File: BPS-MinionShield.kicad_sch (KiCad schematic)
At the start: 78 parts, among them J1 Conn_01x18_Female, J14 TempConn2, J9 TempConn2

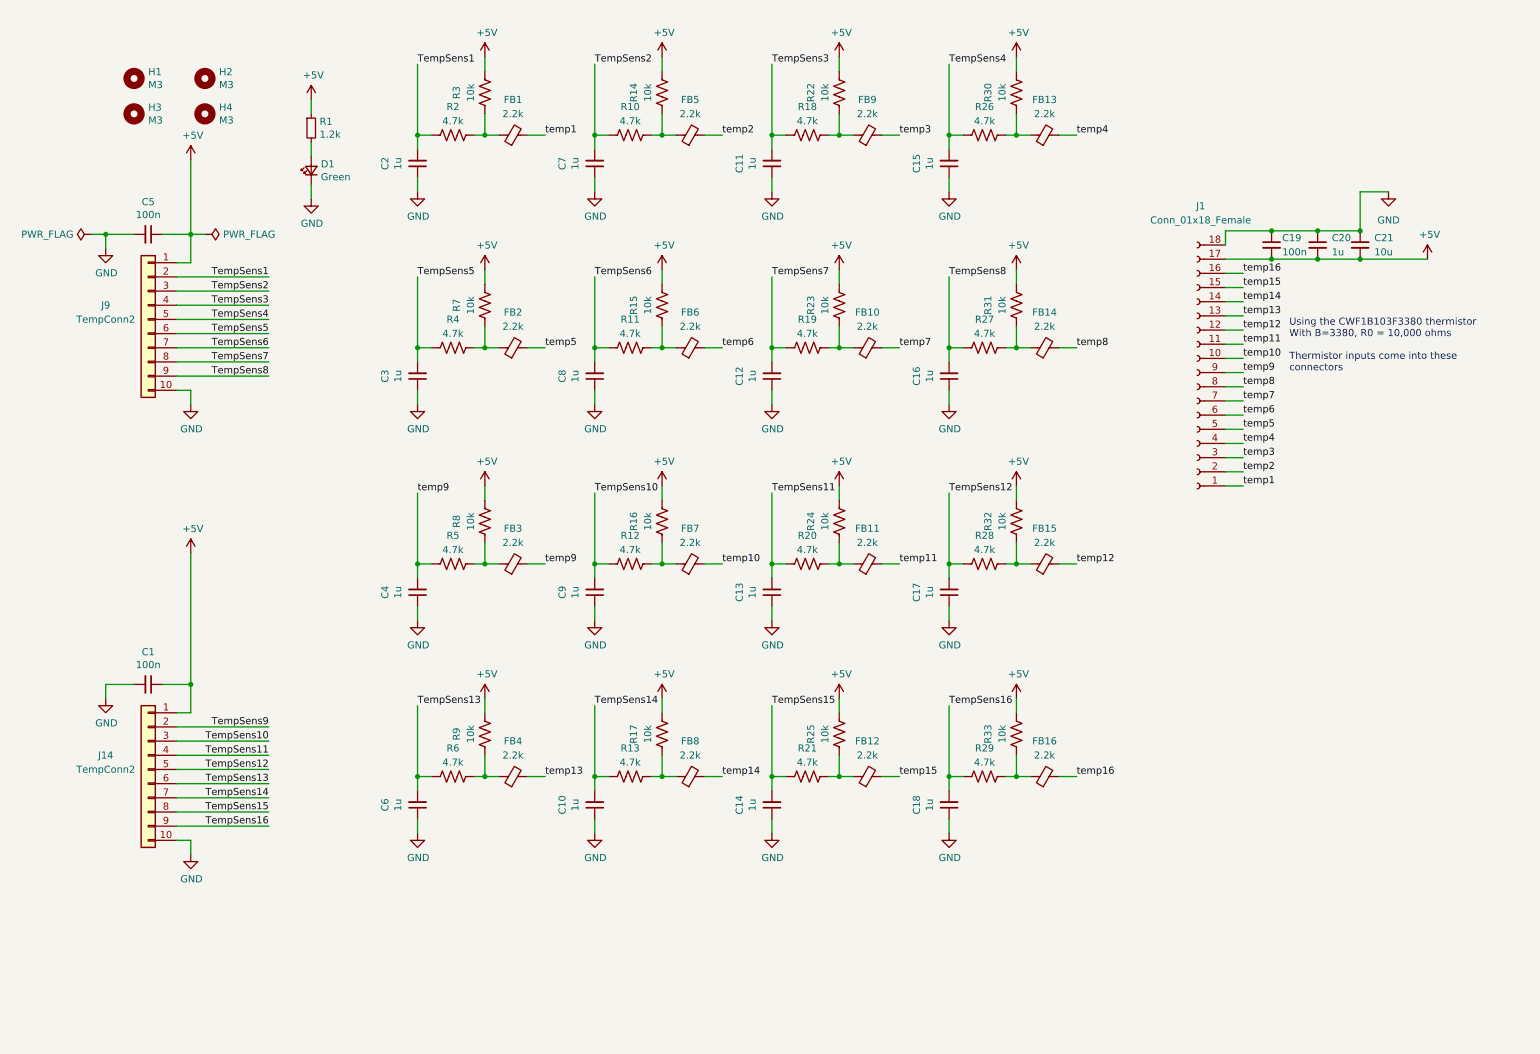
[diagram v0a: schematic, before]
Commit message: added tvs diodes
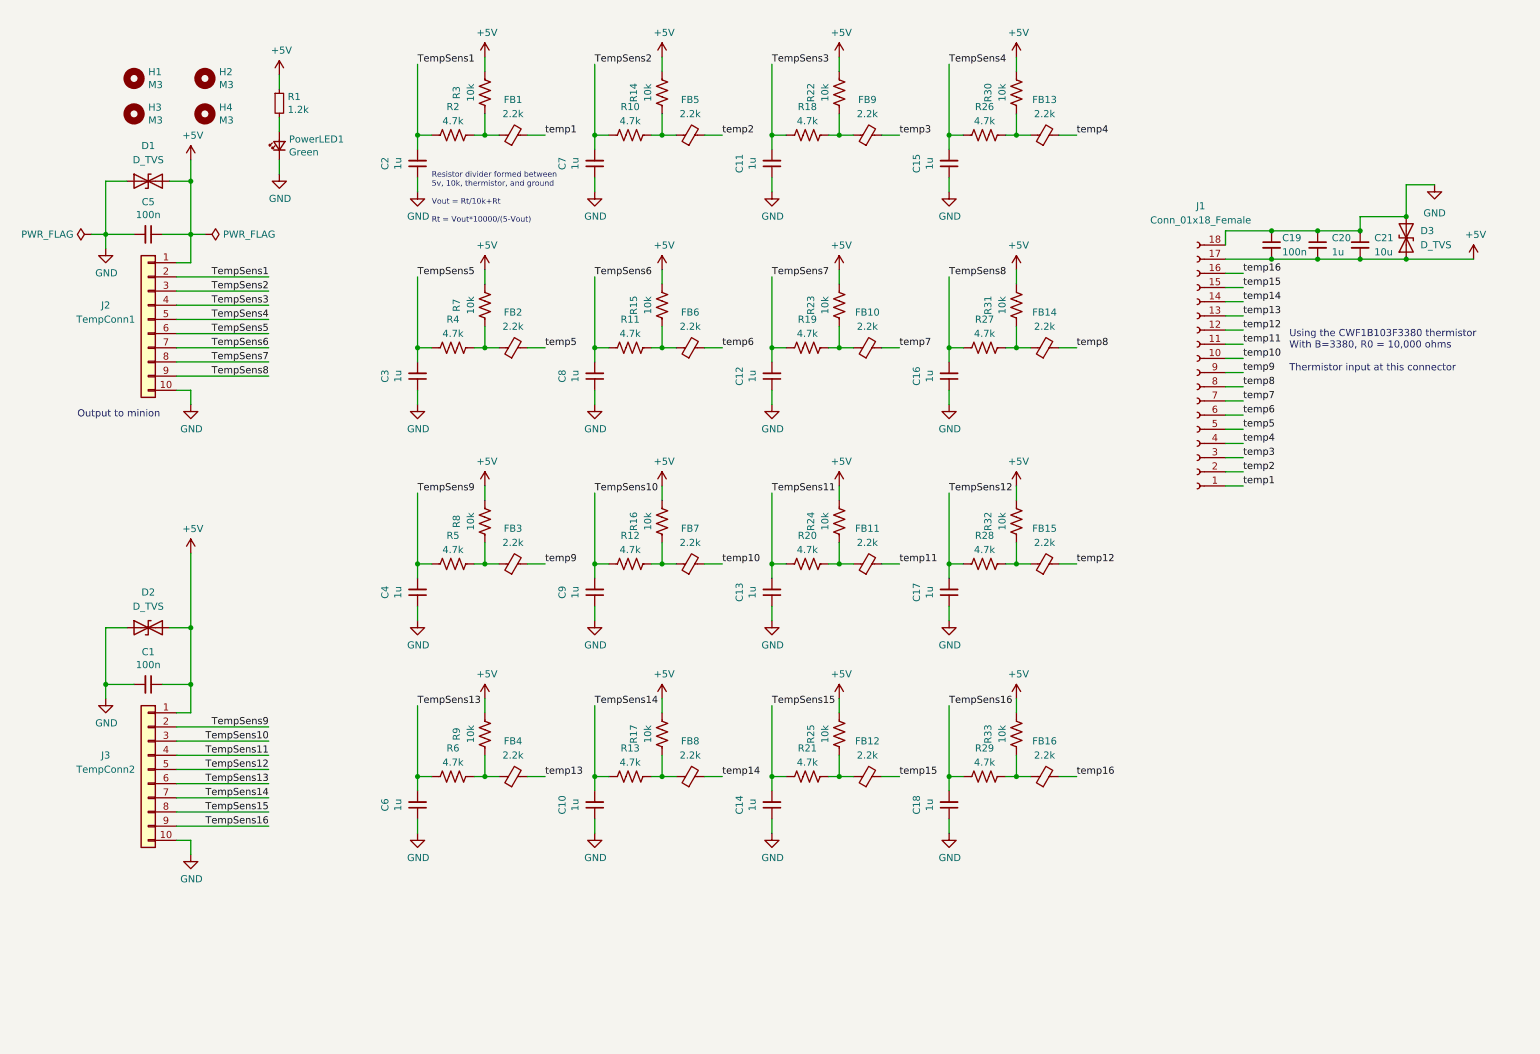
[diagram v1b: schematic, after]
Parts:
- added D1, D2, D3: D_TVS, Diode_SMD:D_0402_1005Metric, symbol Device:D_TVS
- J2: renamed from J9; value TempConn2 -> TempConn1
- renumbered J14 to J3, D1 to PowerLED1
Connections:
- net +5V: now also D1.2 (A2), D2.2 (A2), D3.1 (A1)
- net GND: now also D1.1 (A1), D2.1 (A1), D3.2 (A2)
- net TempSens9: now also C4.2, R5.1
- net temp9: no longer C4.2, R5.1
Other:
- note added: "Output to minion"
- note added: "Resistor divider formed between 5v, 10k, thermistor, and ground Vout = Rt/10k+Rt Rt = Vout*10000/(5-Vout)"
- note added: "Using the CWF1B103F3380 thermistor With B=3380, R0 = 10,000 ohms Thermistor input at this connector"
- note removed: "Using the CWF1B103F3380 thermistor With B=3380, R0 = 10,000 ohms Thermistor inputs come into these connectors"
- moved on the sheet: PowerLED1, R1

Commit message: finished PCB layout with a displayport connector for thermistors
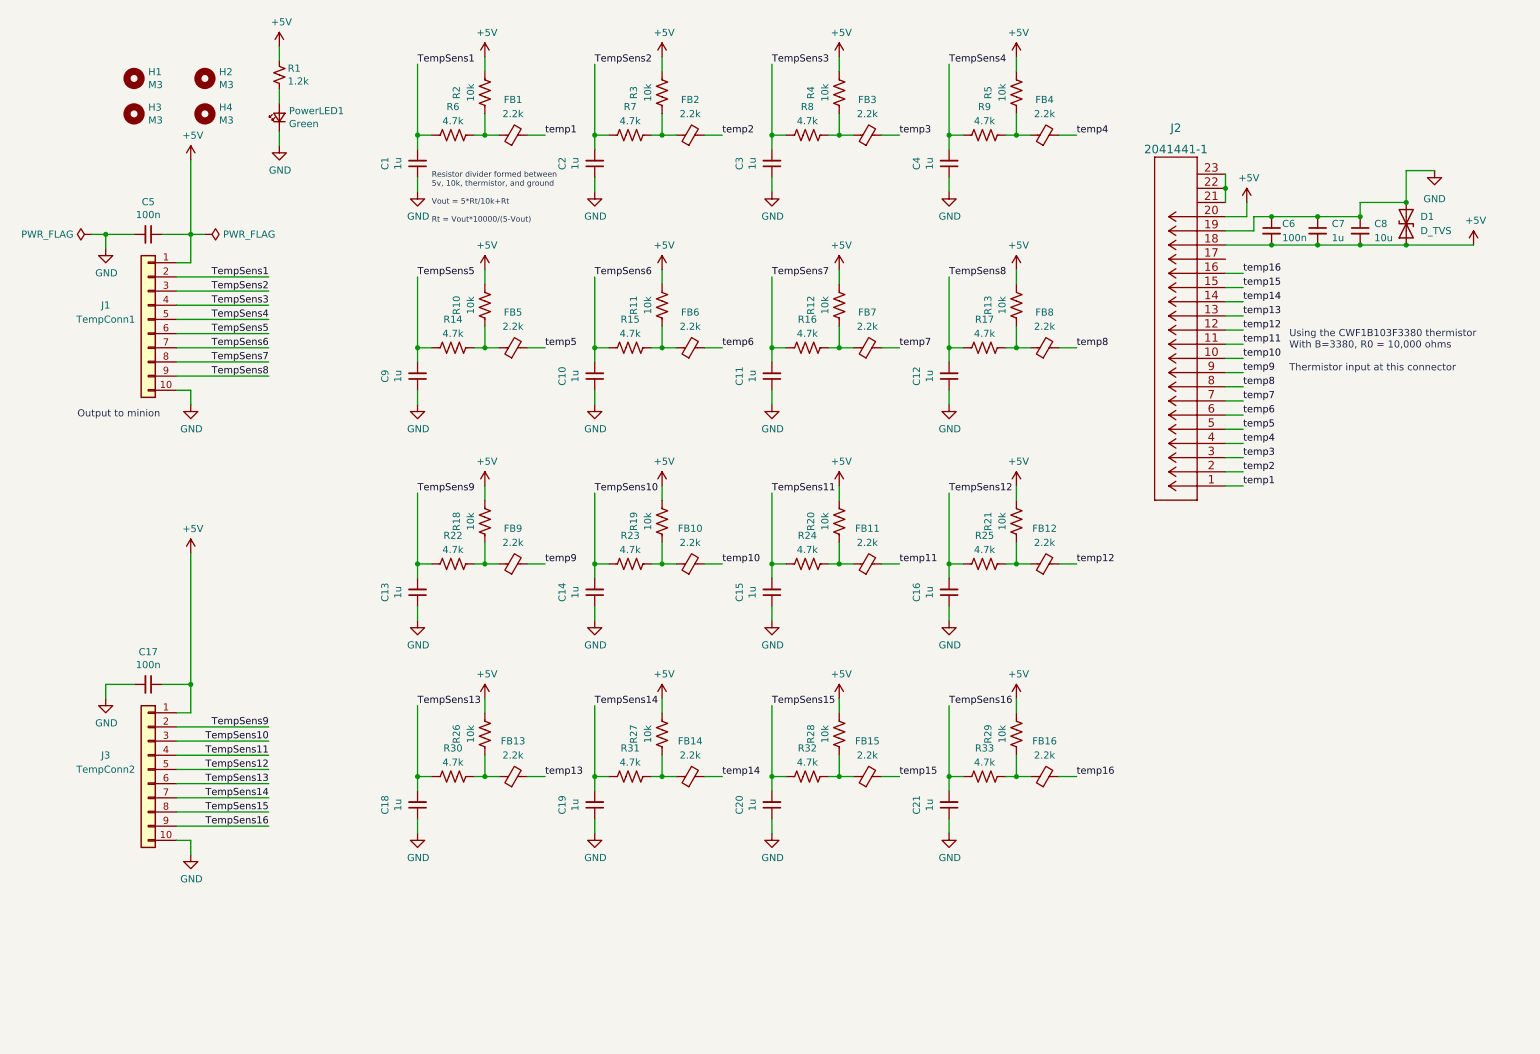
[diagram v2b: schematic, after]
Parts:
- removed D1, D2: D_TVS, Diode_SMD:D_0402_1005Metric, symbol Device:D_TVS
- removed J1: Conn_01x18_Female, symbol Connector:Conn_01x18_Female
- added J2: 2041441-1, UTSVT_Connectors:2041441-1, symbol displayport:2041441-1
- R1: symbol Device:R_Small -> Device:R_Small_US
- renumbered C2 to C1, C8 to C10, C12 to C11, C16 to C12, C4 to C13, C9 to C14, C13 to C15, C17 to C16, C1 to C17, C6 to C18, C10 to C19, C7 to C2, C14 to C20, C18 to C21, C11 to C3, C15 to C4, C19 to C6, C20 to C7, C21 to C8, C3 to C9, D3 to D1, FB7 to FB10, FB15 to FB12, FB4 to FB13, FB8 to FB14, FB12 to FB15, FB5 to FB2, FB9 to FB3, FB13 to FB4, FB2 to FB5, FB10 to FB7, FB14 to FB8, FB3 to FB9, J2 to J1, R7 to R10, R15 to R11, R23 to R12, R31 to R13, R4 to R14, R11 to R15, R19 to R16, R27 to R17, R8 to R18, R16 to R19, R3 to R2, R24 to R20, R32 to R21, R5 to R22, R12 to R23, R20 to R24, R28 to R25, R9 to R26, R17 to R27, R25 to R28, R33 to R29, R14 to R3, R6 to R30, R13 to R31, R21 to R32, R29 to R33, R22 to R4, R30 to R5, R2 to R6, R10 to R7, R18 to R8, R26 to R9
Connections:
- net +5V: now also J2.18, J2.20
- net GND: now also J2.19
- net temp1: now also J2.1
- net temp10: now also J2.10
- net temp11: now also J2.11
- net temp12: now also J2.12
- net temp13: now also J2.13
- net temp14: now also J2.14
- net temp15: now also J2.15
- net temp16: now also J2.16
- net temp2: now also J2.2
- net temp3: now also J2.3
- net temp4: now also J2.4
- net temp5: now also J2.5
- net temp6: now also J2.6
- net temp7: now also J2.7
- net temp8: now also J2.8
- net temp9: now also J2.9
- new net: J2.21 (SHIELD), J2.22 (SHIELD), J2.23 (SHIELD)
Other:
- note added: "Resistor divider formed between 5v, 10k, thermistor, and ground Vout = 5*Rt/10k+Rt Rt = Vout*10000/(5-Vout)"
- note removed: "Resistor divider formed between 5v, 10k, thermistor, and ground Vout = Rt/10k+Rt Rt = Vout*10000/(5-Vout)"
- title: (none) -> MinionShield
- moved on the sheet: C6, C7, C8, D1, PowerLED1

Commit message: added orion connector footprint
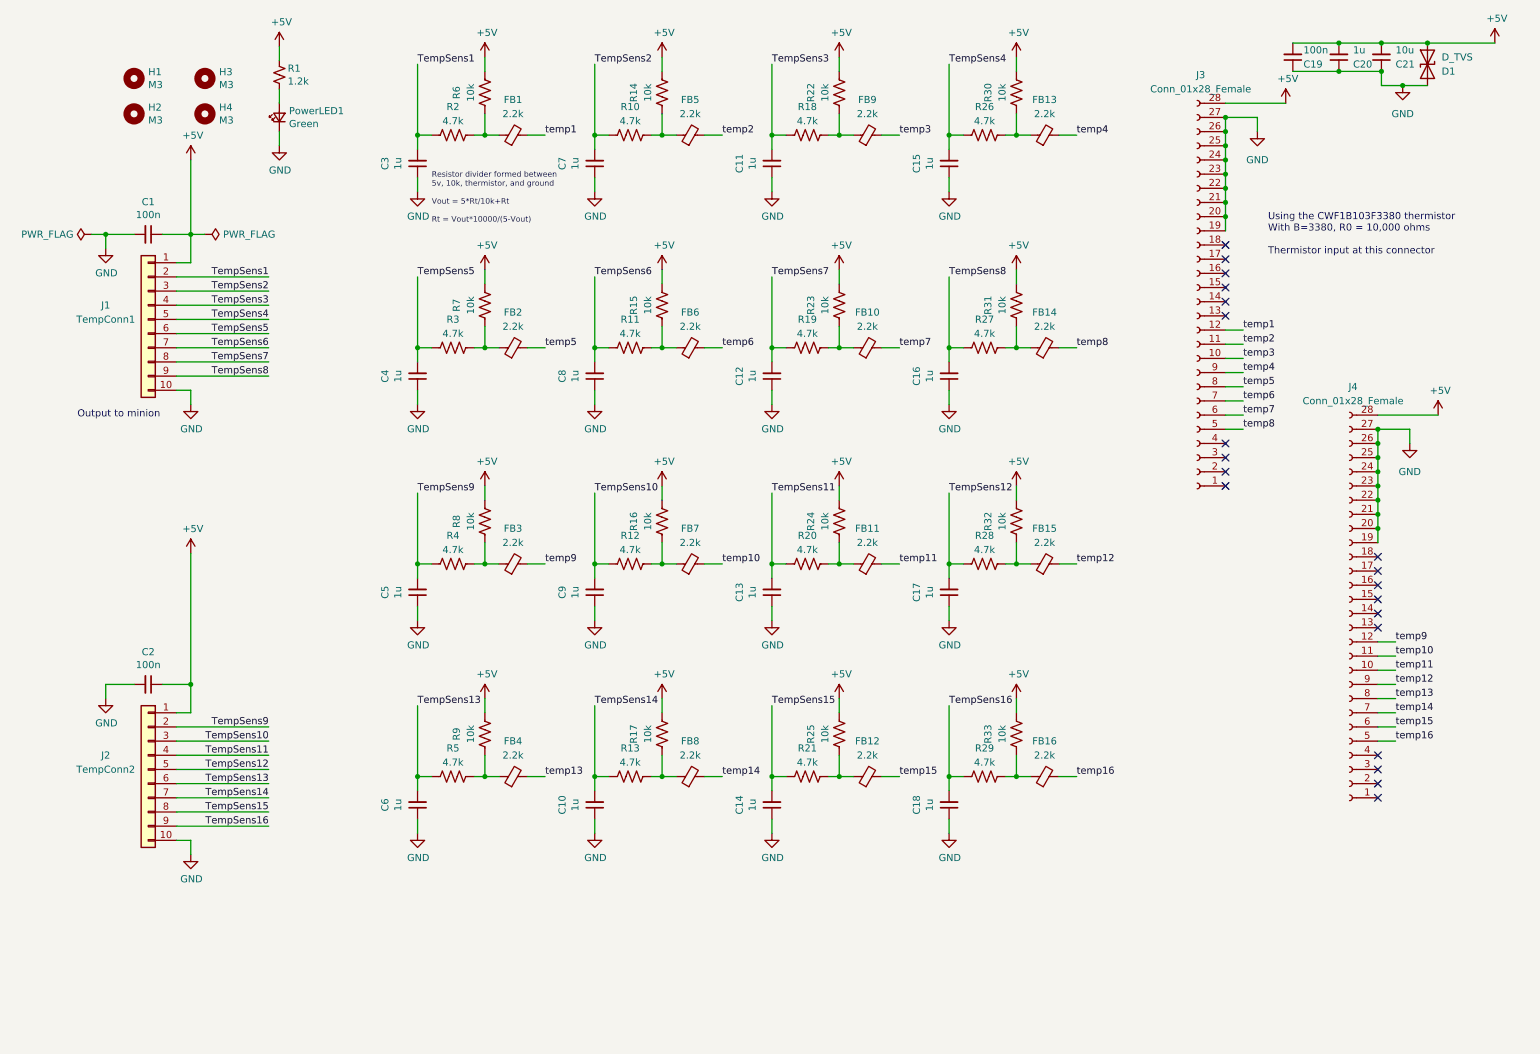
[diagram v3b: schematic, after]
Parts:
- removed J2: 2041441-1, UTSVT_Connectors:2041441-1, symbol displayport:2041441-1
- added J3, J4: Conn_01x28_Female, UTSVT_Connectors:MX34028SF1, symbol Connector:Conn_01x28_Female
- renumbered C5 to C1, C19 to C10, C3 to C11, C11 to C12, C15 to C13, C20 to C14, C4 to C15, C12 to C16, C16 to C17, C21 to C18, C6 to C19, C17 to C2, C7 to C20, C8 to C21, C1 to C3, C9 to C4, C13 to C5, C18 to C6, C2 to C7, C10 to C8, C14 to C9, FB7 to FB10, FB15 to FB12, FB4 to FB13, FB8 to FB14, FB12 to FB15, FB5 to FB2, FB9 to FB3, FB13 to FB4, FB2 to FB5, FB10 to FB7, FB14 to FB8, FB3 to FB9, H3 to H2, H2 to H3, J3 to J2, R7 to R10, R15 to R11, R23 to R12, R31 to R13, R3 to R14, R11 to R15, R19 to R16, R27 to R17, R8 to R18, R16 to R19, R6 to R2, R24 to R20, R32 to R21, R4 to R22, R12 to R23, R20 to R24, R28 to R25, R9 to R26, R17 to R27, R25 to R28, R33 to R29, R14 to R3, R5 to R30, R13 to R31, R21 to R32, R29 to R33, R22 to R4, R30 to R5, R2 to R6, R10 to R7, R18 to R8, R26 to R9
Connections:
- net +5V: now also J3.28 (Pin_28), J4.28 (Pin_28)
- net GND: now also J3.19 (Pin_19), J3.20 (Pin_20), J3.21 (Pin_21), J3.22 (Pin_22), J3.23 (Pin_23), J3.24 (Pin_24), J3.25 (Pin_25), J3.26 (Pin_26), J3.27 (Pin_27), J4.19 (Pin_19), J4.20 (Pin_20), J4.21 (Pin_21), J4.22 (Pin_22), J4.23 (Pin_23), J4.24 (Pin_24), J4.25 (Pin_25), J4.26 (Pin_26), J4.27 (Pin_27)
- net temp1: now also J3.12 (Pin_12)
- net temp10: now also J4.11 (Pin_11)
- net temp11: now also J4.10 (Pin_10)
- net temp12: now also J4.9 (Pin_9)
- net temp13: now also J4.8 (Pin_8)
- net temp14: now also J4.7 (Pin_7)
- net temp15: now also J4.6 (Pin_6)
- net temp16: now also J4.5 (Pin_5)
- net temp2: now also J3.11 (Pin_11)
- net temp3: now also J3.10 (Pin_10)
- net temp4: now also J3.9 (Pin_9)
- net temp5: now also J3.8 (Pin_8)
- net temp6: now also J3.7 (Pin_7)
- net temp7: now also J3.6 (Pin_6)
- net temp8: now also J3.5 (Pin_5)
- net temp9: now also J4.12 (Pin_12)
- no-connect marks 0 -> 20
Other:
- moved on the sheet: C19, C20, C21, D1

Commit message: new footprint from temp expansion module
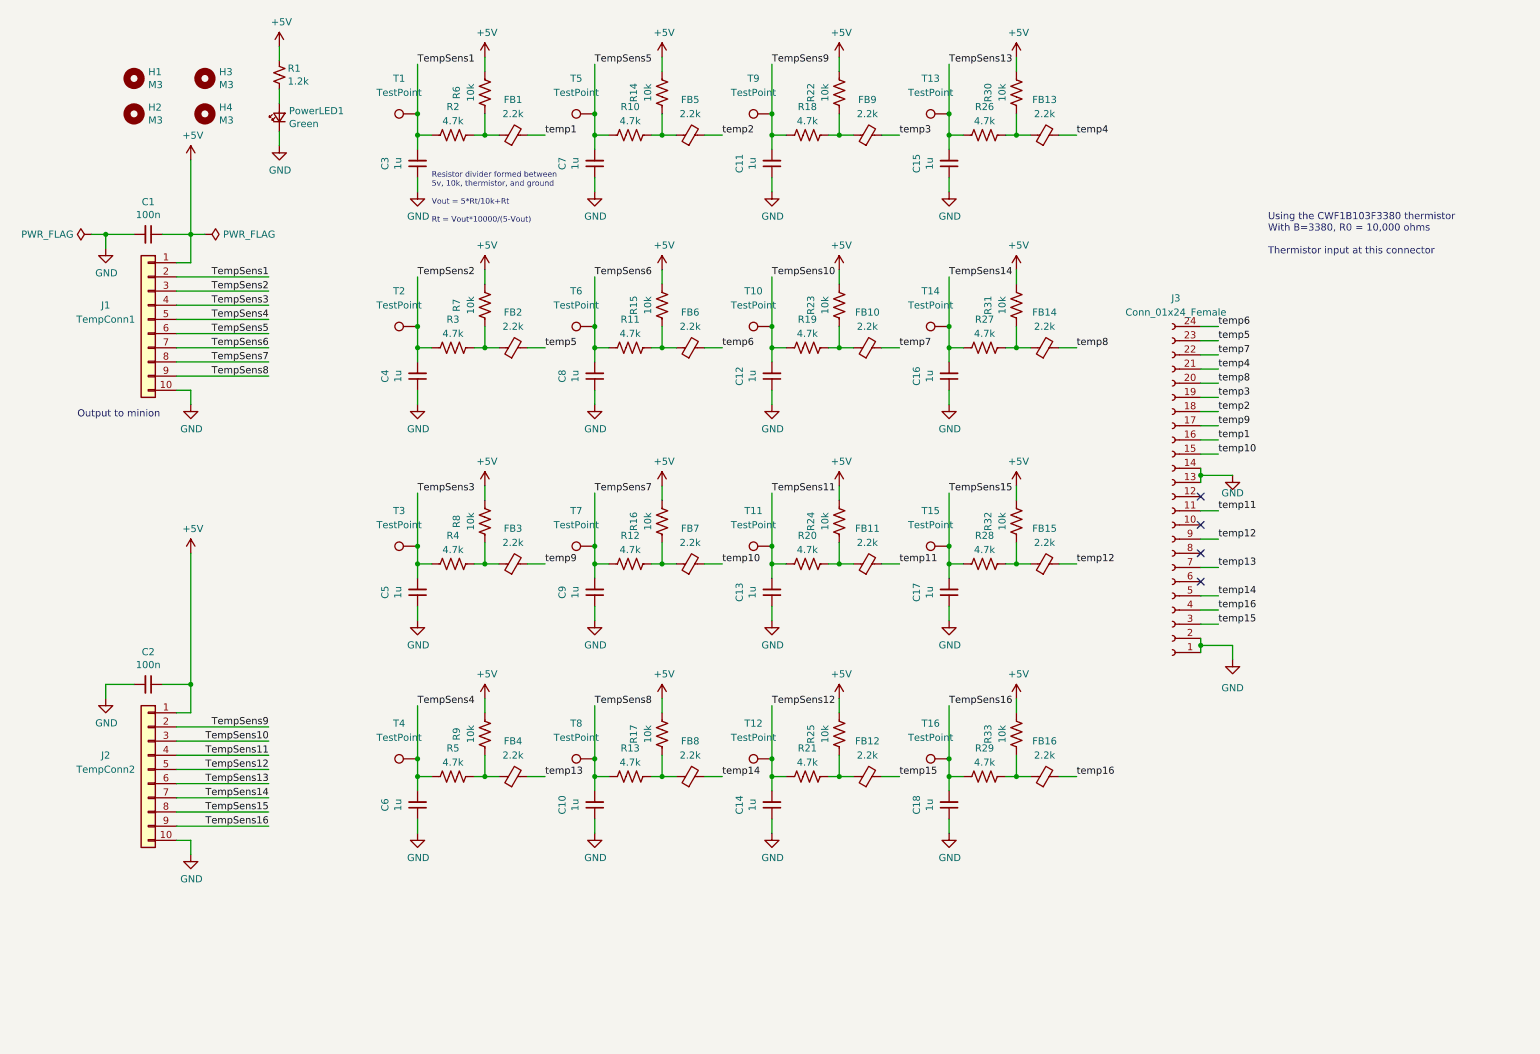
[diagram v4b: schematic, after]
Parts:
- removed C19: 100n, Capacitor_SMD:C_0805_2012Metric, symbol Device:C_Small
- removed C20: 1u, Capacitor_SMD:C_0805_2012Metric, symbol Device:C_Small
- removed C21: 10u, Capacitor_SMD:C_0805_2012Metric, symbol Device:C_Small
- removed D1: D_TVS, Diode_SMD:D_0402_1005Metric, symbol Device:D_TVS
- removed J3, J4: Conn_01x28_Female, UTSVT_Connectors:MX34028SF1, symbol Connector:Conn_01x28_Female
- added J3: Conn_01x24_Female, UTSVT_Connectors:PADP-24V-1-S, symbol Connector:Conn_01x24_Female
- added T1, T10, T11, T12, T13, T14, T15, T16, T2, T3, T4, T5, T6, T7, T8, T9: TestPoint, TestPoint:TestPoint_THTPad_D1.5mm_Drill0.7mm, symbol Connector:TestPoint
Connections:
- net GND: now also J3.1 (Pin_1), J3.13 (Pin_13), J3.14 (Pin_14), J3.2 (Pin_2)
- net TempSens1: now also T1.1
- net TempSens10: now also C12.2, R19.1, T10.1; no longer C9.2, R12.1
- net TempSens11: now also T11.1
- net TempSens12: now also C14.2, R21.1, T12.1; no longer C17.2, R28.1
- net TempSens13: now also C15.2, R26.1, T13.1; no longer C6.2, R5.1
- net TempSens14: now also C16.2, R27.1, T14.1; no longer C10.2, R13.1
- net TempSens15: now also C17.2, R28.1, T15.1; no longer C14.2, R21.1
- net TempSens16: now also T16.1
- net TempSens2: now also C4.2, R3.1, T2.1; no longer C7.2, R10.1
- net TempSens3: now also C5.2, R4.1, T3.1; no longer C11.2, R18.1
- net TempSens4: now also C6.2, R5.1, T4.1; no longer C15.2, R26.1
- net TempSens5: now also C7.2, R10.1, T5.1; no longer C4.2, R3.1
- net TempSens6: now also T6.1
- net TempSens7: now also C9.2, R12.1, T7.1; no longer C12.2, R19.1
- net TempSens8: now also C10.2, R13.1, T8.1; no longer C16.2, R27.1
- net TempSens9: now also C11.2, R18.1, T9.1; no longer C5.2, R4.1
- net temp1: now also J3.16 (Pin_16)
- net temp10: now also J3.15 (Pin_15)
- net temp11: now also J3.11 (Pin_11)
- net temp12: now also J3.9 (Pin_9)
- net temp13: now also J3.7 (Pin_7)
- net temp14: now also J3.5 (Pin_5)
- net temp15: now also J3.3 (Pin_3)
- net temp16: now also J3.4 (Pin_4)
- net temp2: now also J3.18 (Pin_18)
- net temp3: now also J3.19 (Pin_19)
- net temp4: now also J3.21 (Pin_21)
- net temp5: now also J3.23 (Pin_23)
- net temp6: now also J3.24 (Pin_24)
- net temp7: now also J3.22 (Pin_22)
- net temp8: now also J3.20 (Pin_20)
- net temp9: now also J3.17 (Pin_17)
- no-connect marks 20 -> 4
